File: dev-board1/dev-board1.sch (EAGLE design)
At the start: 192 parts, among them IC1 MSP432E401, IC10 CC3120MOD, IC11 4066D, IC2 MT48LC16M16A2, IC3 SIM800C, IC4 OPAMP-DUALU, IC5 TPD3E001DRL, IC6 TPD3E001DRL, IC7 TPD3E001DRL, IC8 BQ25601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

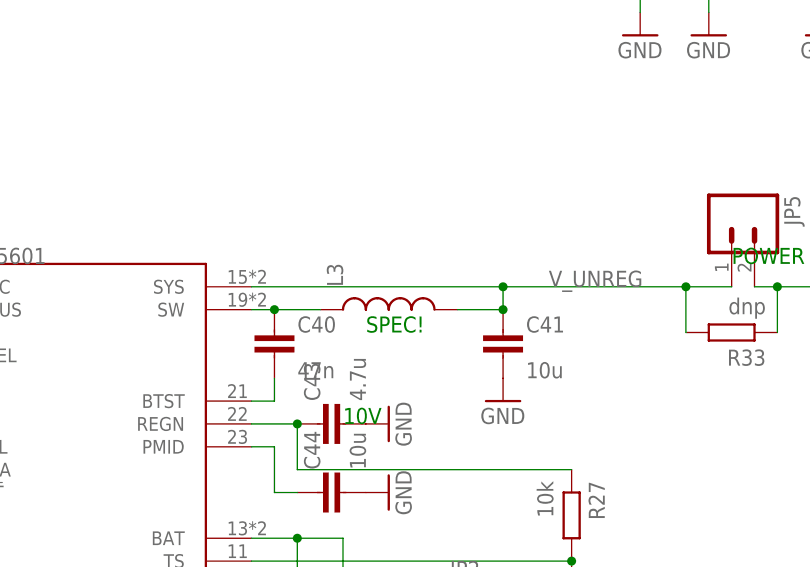
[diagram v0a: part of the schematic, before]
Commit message: adding final few farnell numbers
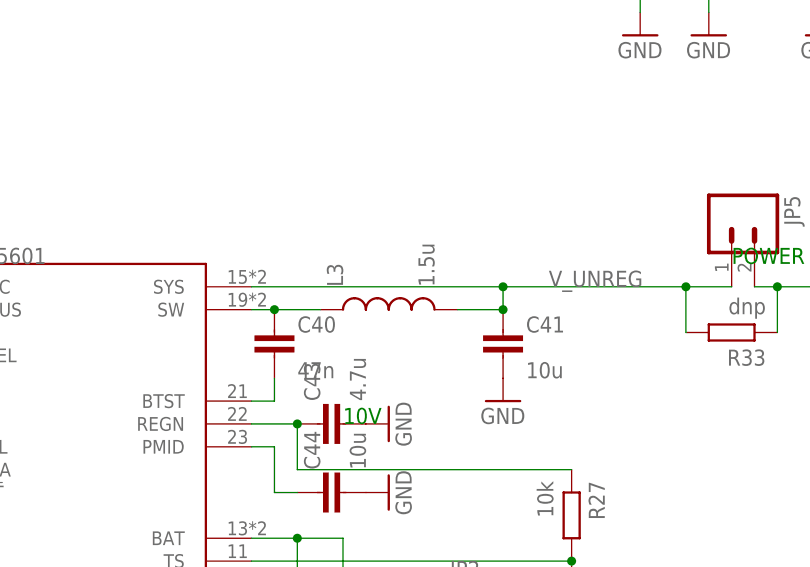
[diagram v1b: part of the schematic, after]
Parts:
- ANT1, ANT2: FARNELL (none) -> 2148522
- C34, C43, C50: FARNELL (none) -> 2524873
- C41, C42, C44, C45, C46, C47: FARNELL (none) -> 2112853/2362101/2576756
- IC4: FARNELL (none) -> 2463666
- J4: FARNELL (none) -> 1865285
- JP15: FARNELL (none) -> 1316987
- JP2: FARNELL (none) -> 9492615
- L3: value (none) -> 1.5u
- X2: FARNELL (none) -> 1248990
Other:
- note removed: "SPEC!"
